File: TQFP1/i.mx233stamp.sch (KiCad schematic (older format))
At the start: 0 parts

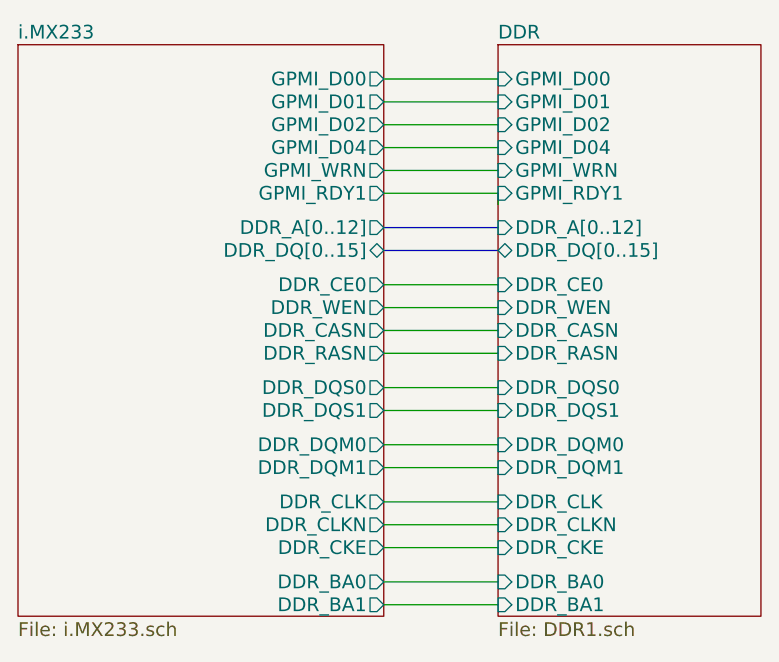
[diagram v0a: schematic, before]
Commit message: PCB labels, improvements 15/04/11
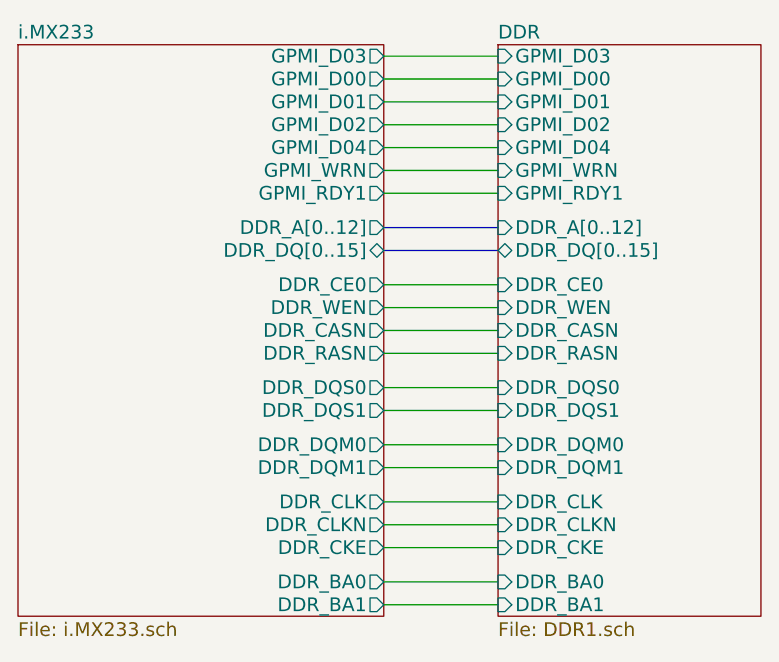
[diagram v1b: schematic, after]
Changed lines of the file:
@@
-EESchema Schematic File Version 2  date Mon 11 Apr 2011 03:43:24 PM COT
+EESchema Schematic File Version 2  date Fri 15 Apr 2011 03:10:43 PM COT
+LIBS:con-jack
 LIBS:adm3101e
 LIBS:microsd
@@
 Sheet 1 3
 Title ""
-Date "11 apr 2011"
+Date "15 apr 2011"
 Rev ""
 Comp ""
@@
 $EndDescr
 Wire Wire Line
-	4750 2150 5250 2150
+	4750 1650 5250 1650
 Wire Wire Line
-	4750 1850 5250 1850
+	4750 2250 5250 2250
+Wire Wire Line
+	5250 1950 4750 1950
+Wire Wire Line
+	5250 1750 4750 1750
+Wire Bus Line
+	5250 2400 4750 2400
+Wire Wire Line
+	4750 3450 5250 3450
+Wire Wire Line
+	5250 3200 4750 3200
+Wire Wire Line
+	4750 2950 5250 2950
+Wire Wire Line
+	4750 4050 5250 4050
+Wire Wire Line
+	4750 3800 5250 3800
+Wire Wire Line
+	4750 3600 5250 3600
+Wire Wire Line
+	4750 2850 5250 2850
+Wire Wire Line
+	4750 2750 5250 2750
+Wire Wire Line
+	4750 2650 5250 2650
+Wire Wire Line
+	4750 3700 5250 3700
+Wire Wire Line
+	4750 3950 5250 3950
+Wire Wire Line
+	4750 3100 5250 3100
+Wire Wire Line
+	5250 3350 4750 3350
+Wire Wire Line
+	4750 2050 5250 2050
 Wire Bus Line
 	4750 2500 5250 2500
 Wire Wire Line
-	4750 2050 5250 2050
+	4750 1850 5250 1850
 Wire Wire Line
-	5250 3350 4750 3350
-Wire Wire Line
-	4750 3100 5250 3100
-Wire Wire Line
-	4750 3950 5250 3950
-Wire Wire Line
-	4750 3700 5250 3700
-Wire Wire Line
-	4750 2650 5250 2650
-Wire Wire Line
-	4750 2750 5250 2750
-Wire Wire Line
-	4750 2850 5250 2850
-Wire Wire Line
-	4750 3600 5250 3600
-Wire Wire Line
-	4750 3800 5250 3800
-Wire Wire Line
-	4750 4050 5250 4050
-Wire Wire Line
-	4750 2950 5250 2950
-Wire Wire Line
-	5250 3200 4750 3200
-Wire Wire Line
-	4750 3450 5250 3450
-Wire Bus Line
-	5250 2400 4750 2400
-Wire Wire Line
-	5250 1750 4750 1750
-Wire Wire Line
-	5250 1950 4750 1950
-Wire Wire Line
-	5250 2300 5250 2250
-Wire Wire Line
-	5250 2250 4750 2250
+	4750 2150 5250 2150
 $Sheet
 S 5250 1600 1150 2500
@@
 F21 "GPMI_D01" I L 5250 1850 60
 F22 "GPMI_D00" I L 5250 1750 60
+F23 "GPMI_D03" I L 5250 1650 60
 $EndSheet
 $Sheet
@@
 F21 "GPMI_D01" O R 4750 1850 60
 F22 "GPMI_D02" O R 4750 1950 60
+F23 "GPMI_D03" O R 4750 1650 60
 $EndSheet
 $EndSCHEMATC
